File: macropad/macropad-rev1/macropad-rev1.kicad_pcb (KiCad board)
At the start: 2 copper layers, 136 x 61 mm, 30 parts, among them Q1 2N7000, Q2 2N7000, Q3 2N7000, Q4 2N7000, SW10 RotaryEncoder_Switch, U1 Pico, U2 MDOB128032GV-WI

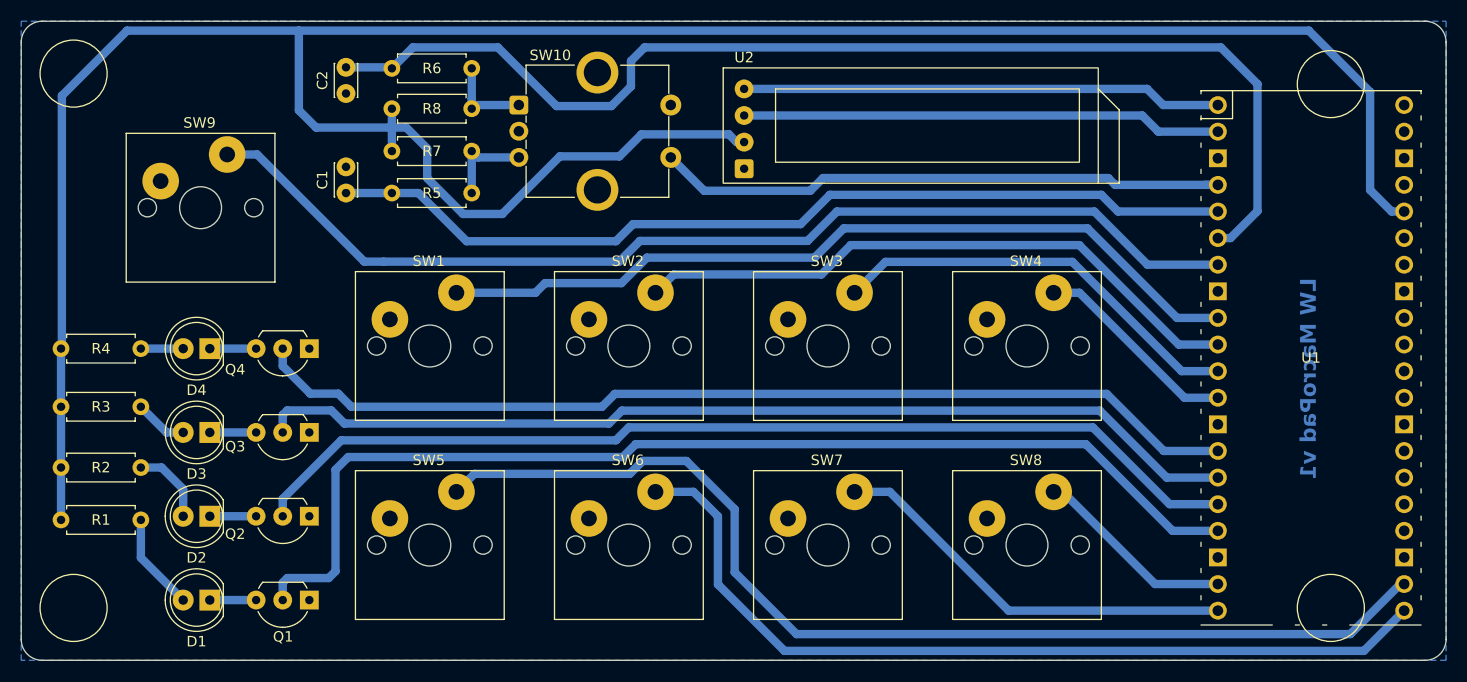
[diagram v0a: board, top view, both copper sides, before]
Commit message: Now using SVG and drill marks
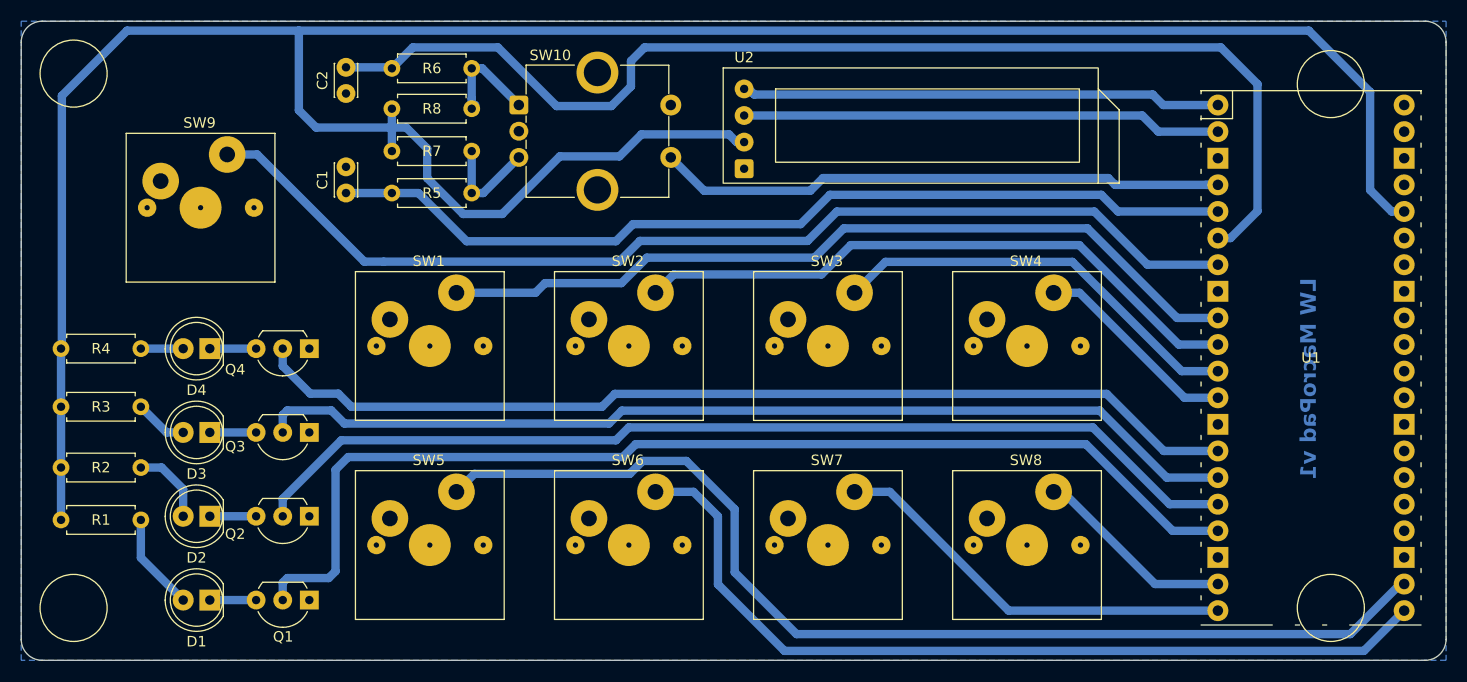
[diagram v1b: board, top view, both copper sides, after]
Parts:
- SW1, SW2, SW3, SW4, SW5, SW6, SW7, SW8, SW9: footprint LiveWires:LW_CherrySwitch -> LiveWires:LW_CherrySwitch_DrillMarks
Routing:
- net Net-(R6-Pad1): track 8.49 -> 10.3 mm
- net Net-(R5-Pad1): track 8.75 -> 9.91 mm

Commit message: Working PCB
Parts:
- SW1, SW2, SW3, SW4, SW5, SW6, SW7, SW8, SW9: footprint LiveWires:LW_CherrySwitch_DrillMarks -> LiveWires:LW_CherrySwitch
- moved C2 33.0 mm to (150.0, 76.5)
- moved C1 3.94 mm to (115.0, 82.0)
- moved R1 2.40 mm to (97.4, 119.0)
- moved R6 2.19 mm to (127.0, 74.4)
- moved R8 2.19 mm to (119.4, 78.2)
- moved SW10 2.19 mm to (131.5, 77.9)
- moved R5 2.19 mm to (127.0, 86.3)
- moved R7 2.19 mm to (127.0, 82.3)
- moved R2 1.40 mm to (97.4, 113.0)
- moved R3 1.20 mm to (97.4, 107.0)
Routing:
- net Net-(U1-GPIO3): track 87.6 -> 90.9 mm
- net GND: track 0.00 -> 2.67 mm
- net VCC: track 247.3 -> 245.1 mm
- net Net-(U1-GPIO15): track 39.4 -> 41.1 mm
- net Net-(U1-GPIO2): track 55.5 -> 57.1 mm
- net Net-(D1-A): track 9.32 -> 8.22 mm
- net Net-(D2-A): track 7.48 -> 6.43 mm
- net Net-(Q1-G): track 105.5 -> 104.8 mm
- net Net-(Q4-G): track 95.3 -> 95.9 mm
- net Net-(U1-GPIO4): track 112.3 -> 112.9 mm
- net Net-(U1-GPIO17): track 104.0 -> 104.5 mm
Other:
- board text added: "Readable on Lightbox"
- board text added: "Readable on PCB"
